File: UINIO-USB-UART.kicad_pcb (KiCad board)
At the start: 2 copper layers, 72.2 x 20.5 mm, 42 parts, among them J1 Conn_01x08_Male, J2 Conn_01x04_Male, J3 Conn_01x07_Male, J4 Conn_01x06_Male, J5 Conn_01x04_Male, J6 Conn_01x07_Male, SW1 TP-33103, U1 CP2102, U2 CH343P

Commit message: Update PCB design.
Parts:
- SW1: value TP-33103 -> SWITCH_TP33103
- moved C6 0.90 mm to (135.9, 99.4)
- moved C7 0.54 mm to (141.3, 96.0)
- moved C5 0.13 mm to (141.3, 103.8)
- moved SW1 0.12 mm to (133.5, 107.4)
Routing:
- net /CH343_VDD_5V: track 59.2 -> 60.8 mm
- net /CH343_VIO: track 49.9 -> 49.0 mm
- net /CH343_ACT#: track 7.45 -> 8.17 mm
- net GND: track 278.7 -> 278.4 mm, vias 21 -> 24

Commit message: Update PCB logo.
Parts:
- moved ? 1.31 mm to (141.4, 99.8)
- moved ? 0.55 mm to (180.1, 99.8)
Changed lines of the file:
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@@
   )
   (footprint "LOGO" (layer "B.Cu")
-    (at 180.6 99.8 180)
+    (at 180.054549 99.837387 180)
     (attr board_only exclude_from_pos_files exclude_from_bom)
     (fp_text reference "" (at 0 0) (layer "B.SilkS")
@@
   )
   (footprint "LOGO" (layer "B.Cu")
-    (at 140.094549 99.717387 180)
+    (at 141.404549 99.797387 180)
     (attr board_only exclude_from_pos_files exclude_from_bom)
     (fp_text reference "" (at 0 0) (layer "B.SilkS")

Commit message: Finish switch version.
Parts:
- added ?: , LOGO, F.Cu at (144.5, 99.8)
- added ?: , LOGO, F.Cu at (187.5, 101.5)
- moved ? 0.42 mm to (141.0, 99.8)
- moved ? 0.30 mm to (180.3, 100.0)
- moved Hole3 0.25 mm to (156.3, 108.3)
- moved Hole7 0.20 mm to (194.8, 108.1)
- moved Hole8 0.14 mm to (194.8, 91.7)
- moved Hole4 0.05 mm to (156.3, 91.6)

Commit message: Finish PinHeader version.
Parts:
- removed SW1: SWITCH_TP33103, Uinio:SW-TH_ROCPU_TP-33103
- added J7: Conn_01x03_Male, Connector_PinHeader_2.54mm:PinHeader_1x03_P2.54mm_Vertical, F.Cu at (130.6, 108.7)
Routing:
- net GND: track 278.4 -> 269.1 mm, vias 24 -> 26
- net /CH343_VDD_3.3V: track 40.1 -> 41.3 mm
- net /CH343_VDD_5V: track 60.8 -> 61.7 mm
- net /CP2102_*SUSPEND: track 12.1 -> 11.3 mm
- net /CH343_ACT#: track 8.17 -> 7.45 mm
- net /CH343_VIO: track 49.0 -> 49.7 mm
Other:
- board text added: "VIO"

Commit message: Release 2.0.0.
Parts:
- removed the ? at (144.5, 99.8)
- removed the ? at (187.5, 101.5)
- added ?: , LOGO, F.Cu at (133.3, 99.9)
- added ?: , LOGO, F.Cu at (187.6, 100.0)
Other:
- board text added: "UINIO-USB-UART-CP2102"
- board text added: "Version 2.0.0"
- board text removed: "UINIO-USB-UART-CCP2102"
- board text removed: "Version 1.0.0"

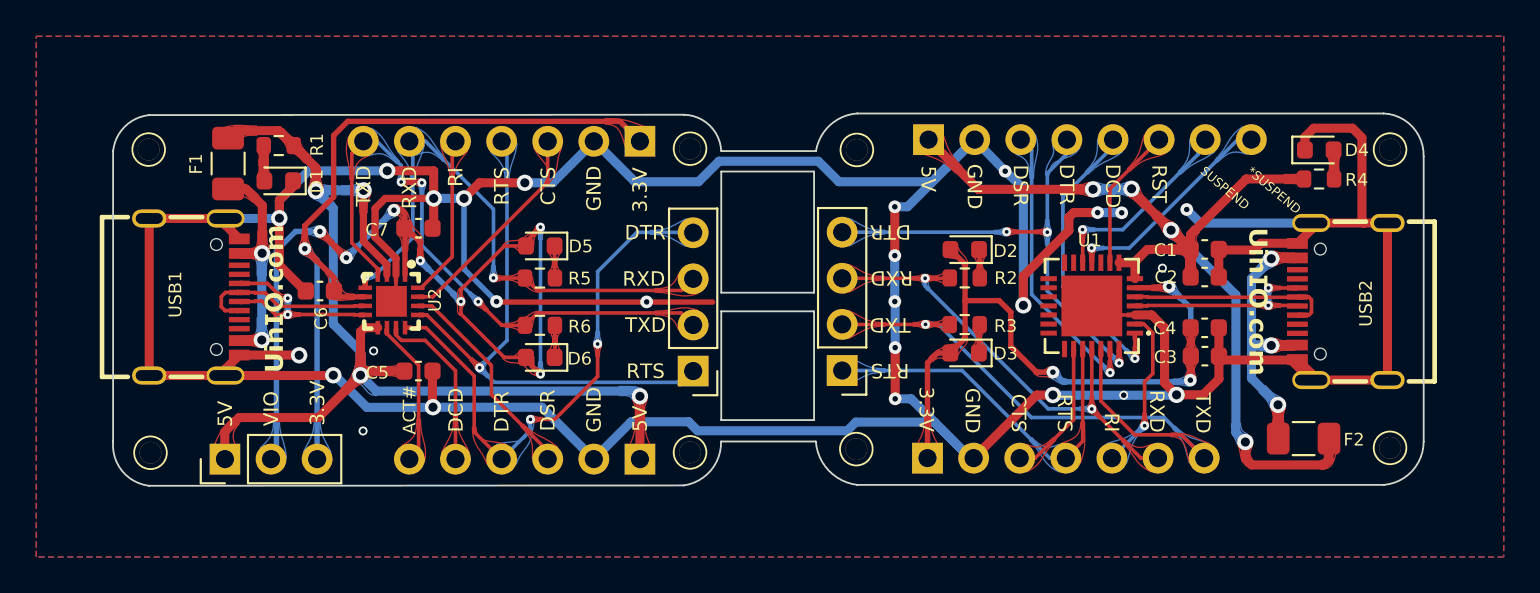
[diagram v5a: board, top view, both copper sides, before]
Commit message: Update threaded hole.
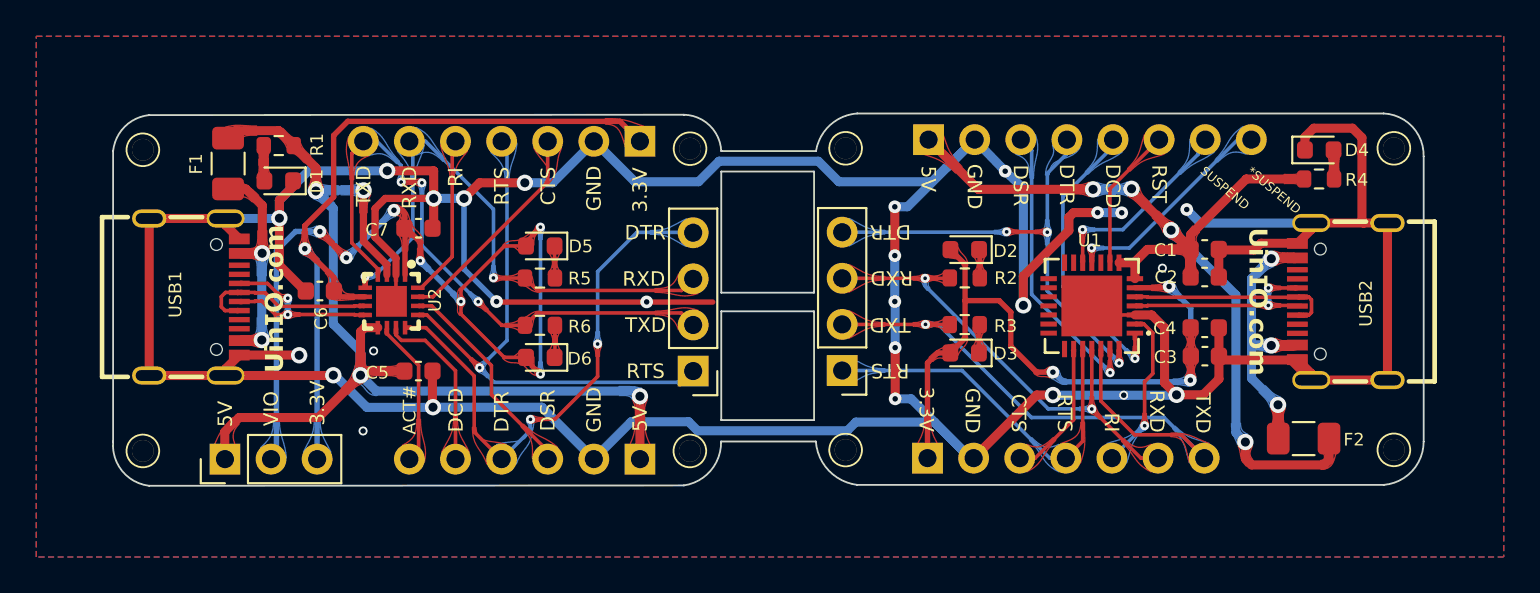
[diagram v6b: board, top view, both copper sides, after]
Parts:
- moved Hole5 0.63 mm to (164.8, 91.6)
- moved Hole6 0.59 mm to (164.8, 108.2)
- moved Hole2 0.43 mm to (126.1, 108.2)
- moved Hole1 0.32 mm to (126.1, 91.7)
- moved Hole7 0.24 mm to (195.0, 108.2)
- moved Hole8 0.22 mm to (195.0, 91.6)
- moved Hole3 0.08 mm to (156.2, 108.2)
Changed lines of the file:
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@@
   )
   (footprint "Uinio:Hole-1mm" (layer "F.Cu")
-    (at 126.44 91.65)
+    (at 126.12 91.66)
     (attr through_hole)
     (fp_text reference "Hole1" (at 0 -2 unlocked) (layer "F.SilkS") hide
@@
   )
   (footprint "Uinio:Hole-1mm" (layer "F.Cu")
-    (at 194.82 91.65)
+    (at 195.03 91.58)
     (attr through_hole)
     (fp_text reference "Hole8" (at 0 -2 unlocked) (layer "F.SilkS") hide
@@
   )
   (footprint "Uinio:Hole-1mm" (layer "F.Cu")
-    (at 156.26 108.33)
+    (at 156.25 108.25)
     (attr through_hole)
     (fp_text reference "Hole3" (at 0 -2 unlocked) (layer "F.SilkS") hide
@@
   )
   (footprint "Uinio:Hole-1mm" (layer "F.Cu")
-    (at 165.45 91.67)
+    (at 164.83 91.58)
     (attr through_hole)
     (fp_text reference "Hole5" (at 0 -2 unlocked) (layer "F.SilkS") hide
@@
   )
   (footprint "Uinio:Hole-1mm" (layer "F.Cu")
-    (at 126.54 108.35)
+    (at 126.12 108.25)
     (attr through_hole)
     (fp_text reference "Hole2" (at 0 -2 unlocked) (layer "F.SilkS") hide
@@
   )
   (footprint "Uinio:Hole-1mm" (layer "F.Cu")
-    (at 194.82 108.08)
+    (at 195.03 108.19)
     (attr through_hole)
     (fp_text reference "Hole7" (at 0 -2 unlocked) (layer "F.SilkS") hide
@@
   )
   (footprint "Uinio:Hole-1mm" (layer "F.Cu")
-    (at 165.42 108.15)
+    (at 164.83 108.2)
     (attr through_hole)
     (fp_text reference "Hole6" (at 0 -2 unlocked) (layer "F.SilkS") hide
@@
   (gr_rect (start 157.98 100.56) (end 163.09 106.55) (layer "Edge.Cuts") (width 0.1) (fill none))
   (gr_rect (start 124.4325 110.22) (end 157.9275 89.7) (layer "User.1") (width 0.2) (fill none))
+  (gr_rect (start 124.48 108.25) (end 126.12 110.17) (layer "User.1") (width 0.1) (fill none))
+  (gr_rect (start 195.03 108.2) (end 196.67 110.12) (layer "User.1") (width 0.1) (fill none))
+  (gr_rect (start 163.19 89.66) (end 164.83 91.58) (layer "User.1") (width 0.1) (fill none))
+  (gr_rect (start 156.24 108.25) (end 157.88 110.17) (layer "User.1") (width 0.1) (fill none))
+  (gr_rect (start 163.19 108.2) (end 164.83 110.12) (layer "User.1") (width 0.1) (fill none))
+  (gr_rect (start 156.25 89.74) (end 157.89 91.66) (layer "User.1") (width 0.1) (fill none))
+  (gr_rect (start 195.03 89.66) (end 196.67 91.58) (layer "User.1") (width 0.1) (fill none))
   (gr_rect (start 163.1425 110.17) (end 196.7189 89.61) (layer "User.1") (width 0.2) (fill none))
+  (gr_rect (start 124.47 89.75) (end 126.11 91.67) (layer "User.1") (width 0.1) (fill none))
   (gr_text "Version 2.0.0" (at 126.55 99.8 90) (layer "B.SilkS")
     (effects (font (size 0.6 0.6) (thickness 0.1)) (justify mirror))
